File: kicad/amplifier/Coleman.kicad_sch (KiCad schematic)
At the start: 26 parts, among them Q10 STP55NF06L, Q11 STP55NF06L, Q12 STP55NF06L, Q9 STP55NF06L, U5 LM4041LP-ADJ, U6 LM4041LP-ADJ

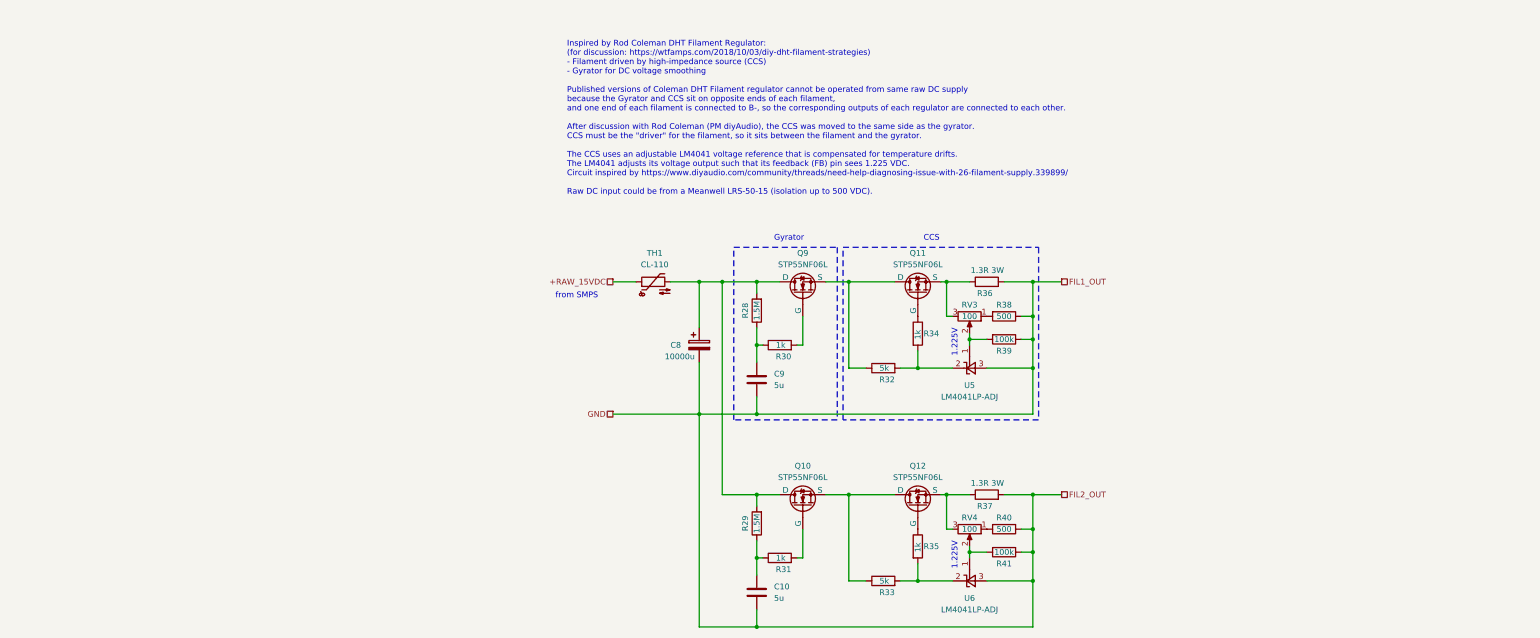
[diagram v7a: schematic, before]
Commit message: LM4041 (noisy!) --> LM431
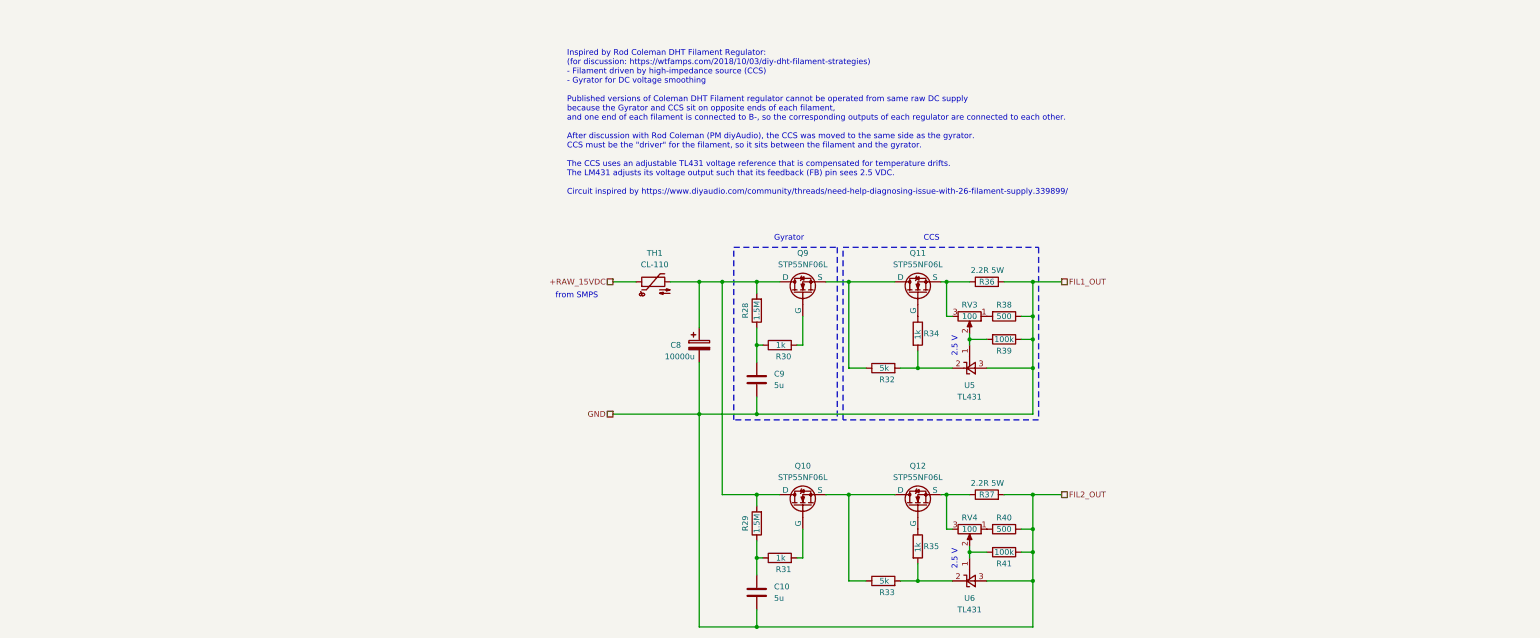
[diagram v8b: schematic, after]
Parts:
- R36, R37: value 1.3R 3W -> 2.2R 5W; footprint Resistor_THT:R_Axial_DIN0617_L17.0mm_D6.0mm_P25.40mm_Horizontal -> (none)
- U5, U6: value LM4041LP-ADJ -> TL431
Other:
- note added: "2.5 V"
- note removed: "1.225V"
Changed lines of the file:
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@@
     (effects (font (size 1.27 1.27)) (justify left bottom))
   )
-  (text "1.225V" (at 176.53 99.06 90)
+  (text "2.5 V" (at 176.53 99.06 90)
     (effects (font (size 1.27 1.27)) (justify left bottom))
   )
-  (text "1.225V" (at 176.53 146.05 90)
+  (text "2.5 V" (at 176.53 146.05 90)
     (effects (font (size 1.27 1.27)) (justify left bottom))
   )
-  (text "Inspired by Rod Coleman DHT Filament Regulator:\n(for discussion: https://wtfamps.com/2018/10/03/diy-dht-filament-strategies)\n- Filament driven by high-impedance source (CCS)\n- Gyrator for DC voltage smoothing\n\nPublished versions of Coleman DHT Filament regulator cannot be operated from same raw DC supply\nbecause the Gyrator and CCS sit on opposite ends of each filament,\nand one end of each filament is connected to B-, so the corresponding outputs of each regulator are connected to each other.\n\nAfter discussion with Rod Coleman (PM diyAudio), the CCS was moved to the same side as the gyrator.\nCCS must be the \"driver\" for the filament, so it sits between the filament and the gyrator.\n\nThe CCS uses an adjustable LM4041 voltage reference that is compensated for temperature drifts.\nThe LM4041 adjusts its voltage output such that its feedback (FB) pin sees 1.225 VDC.\nCircuit inspired by https://www.diyaudio.com/community/threads/need-help-diagnosing-issue-with-26-filament-supply.339899/\n\nRaw DC input could be from a Meanwell LRS-50-15 (isolation up to 500 VDC)."
+  (text "Inspired by Rod Coleman DHT Filament Regulator:\n(for discussion: https://wtfamps.com/2018/10/03/diy-dht-filament-strategies)\n- Filament driven by high-impedance source (CCS)\n- Gyrator for DC voltage smoothing\n\nPublished versions of Coleman DHT Filament regulator cannot be operated from same raw DC supply\nbecause the Gyrator and CCS sit on opposite ends of each filament,\nand one end of each filament is connected to B-, so the corresponding outputs of each regulator are connected to each other.\n\nAfter discussion with Rod Coleman (PM diyAudio), the CCS was moved to the same side as the gyrator.\nCCS must be the \"driver\" for the filament, so it sits between the filament and the gyrator.\n\nThe CCS uses an adjustable TL431 voltage reference that is compensated for temperature drifts.\nThe LM431 adjusts its voltage output such that its feedback (FB) pin sees 2.5 VDC.\n\nCircuit inspired by https://www.diyaudio.com/community/threads/need-help-diagnosing-issue-with-26-filament-supply.339899/"
     (at 90.17 63.5 0)
     (effects (font (size 1.27 1.27)) (justify left bottom))
@@
   (symbol (lib_id "Device:R") (at 182.88 129.54 90) (unit 1)
     (in_bom yes) (on_board yes) (dnp no)
-    (property "Reference" "R37" (at 184.15 132.08 90)
-      (effects (font (size 1.27 1.27)) (justify left))
-    )
-    (property "Value" "1.3R 3W" (at 186.69 127 90)
-      (effects (font (size 1.27 1.27)) (justify left))
-    )
-    (property "Footprint" "Resistor_THT:R_Axial_DIN0617_L17.0mm_D6.0mm_P25.40mm_Horizontal" (at 182.88 131.318 90)
+    (property "Reference" "R37" (at 182.88 129.54 90)
+      (effects (font (size 1.27 1.27)))
+    )
+    (property "Value" "2.2R 5W" (at 186.69 127 90)
+      (effects (font (size 1.27 1.27)) (justify left))
+    )
+    (property "Footprint" "" (at 182.88 131.318 90)
       (effects (font (size 1.27 1.27)) hide)
     )
@@
       (effects (font (size 1.27 1.27)))
     )
-    (property "Value" "LM4041LP-ADJ" (at 179.07 154.94 0)
+    (property "Value" "TL431" (at 179.07 154.94 0)
       (effects (font (size 1.27 1.27)))
     )
@@
   (symbol (lib_id "Device:R") (at 182.88 82.55 90) (unit 1)
     (in_bom yes) (on_board yes) (dnp no)
-    (property "Reference" "R36" (at 184.15 85.09 90)
-      (effects (font (size 1.27 1.27)) (justify left))
-    )
-    (property "Value" "1.3R 3W" (at 186.69 80.01 90)
-      (effects (font (size 1.27 1.27)) (justify left))
-    )
-    (property "Footprint" "Resistor_THT:R_Axial_DIN0617_L17.0mm_D6.0mm_P25.40mm_Horizontal" (at 182.88 84.328 90)
+    (property "Reference" "R36" (at 182.88 82.55 90)
+      (effects (font (size 1.27 1.27)))
+    )
+    (property "Value" "2.2R 5W" (at 186.69 80.01 90)
+      (effects (font (size 1.27 1.27)) (justify left))
+    )
+    (property "Footprint" "" (at 182.88 84.328 90)
       (effects (font (size 1.27 1.27)) hide)
     )
@@
       (effects (font (size 1.27 1.27)))
     )
-    (property "Value" "LM4041LP-ADJ" (at 179.07 107.95 0)
-      (effects (font (size 1.27 1.27)))
-    )
+    (property "Value" "TL431" (at 179.07 107.95 0)
+      (effects (font (size 1.27 1.27)))
+    )
